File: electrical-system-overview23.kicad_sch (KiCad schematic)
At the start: 20 parts

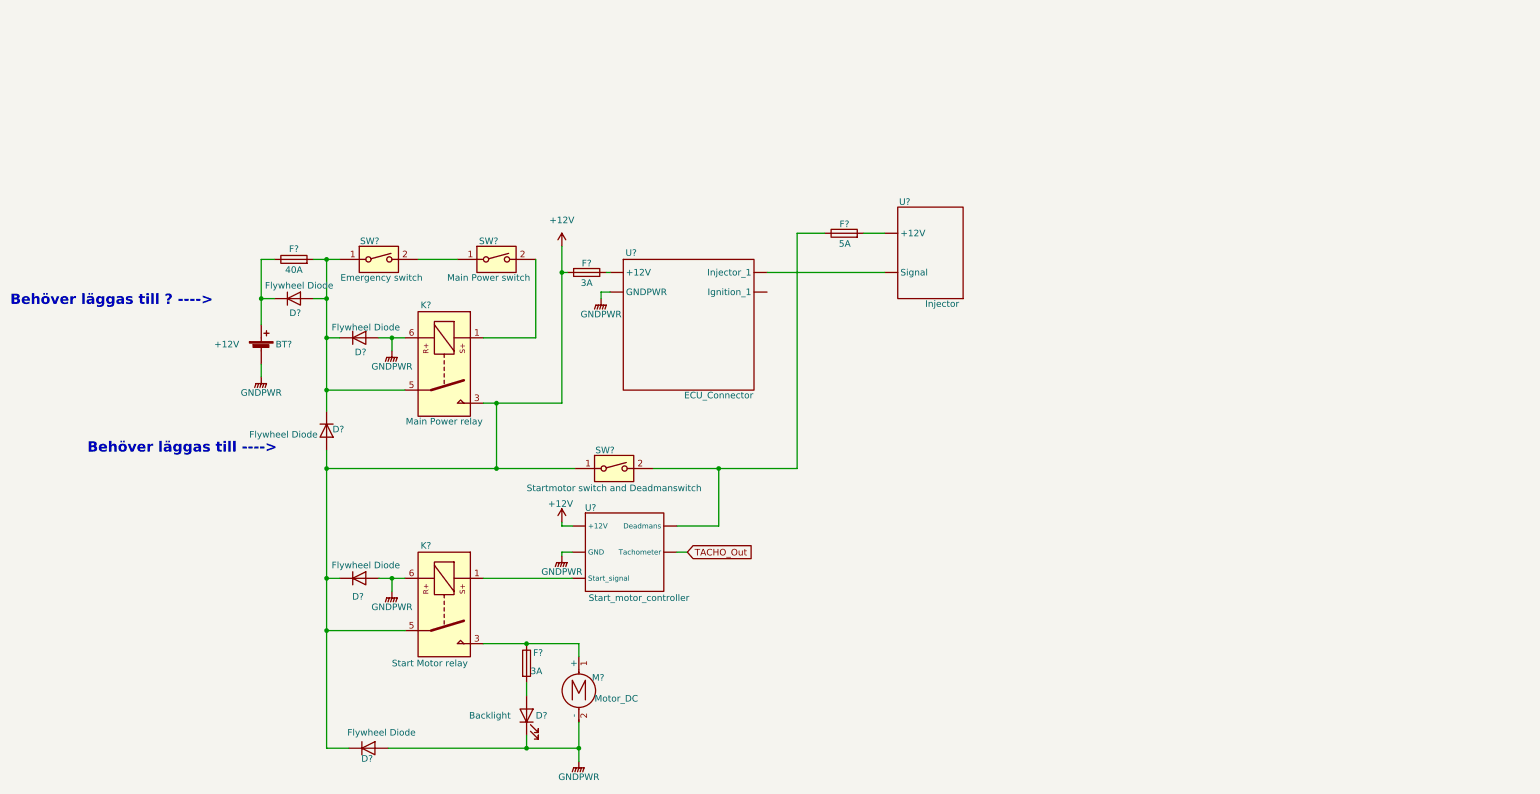
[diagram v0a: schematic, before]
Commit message: Fixed accuracy of system representation
- Changed position for flywheel diode
- Added more components to create a fuller picture
- Restructured the layout for easier reading
- Used two horizontal lines for power and ground
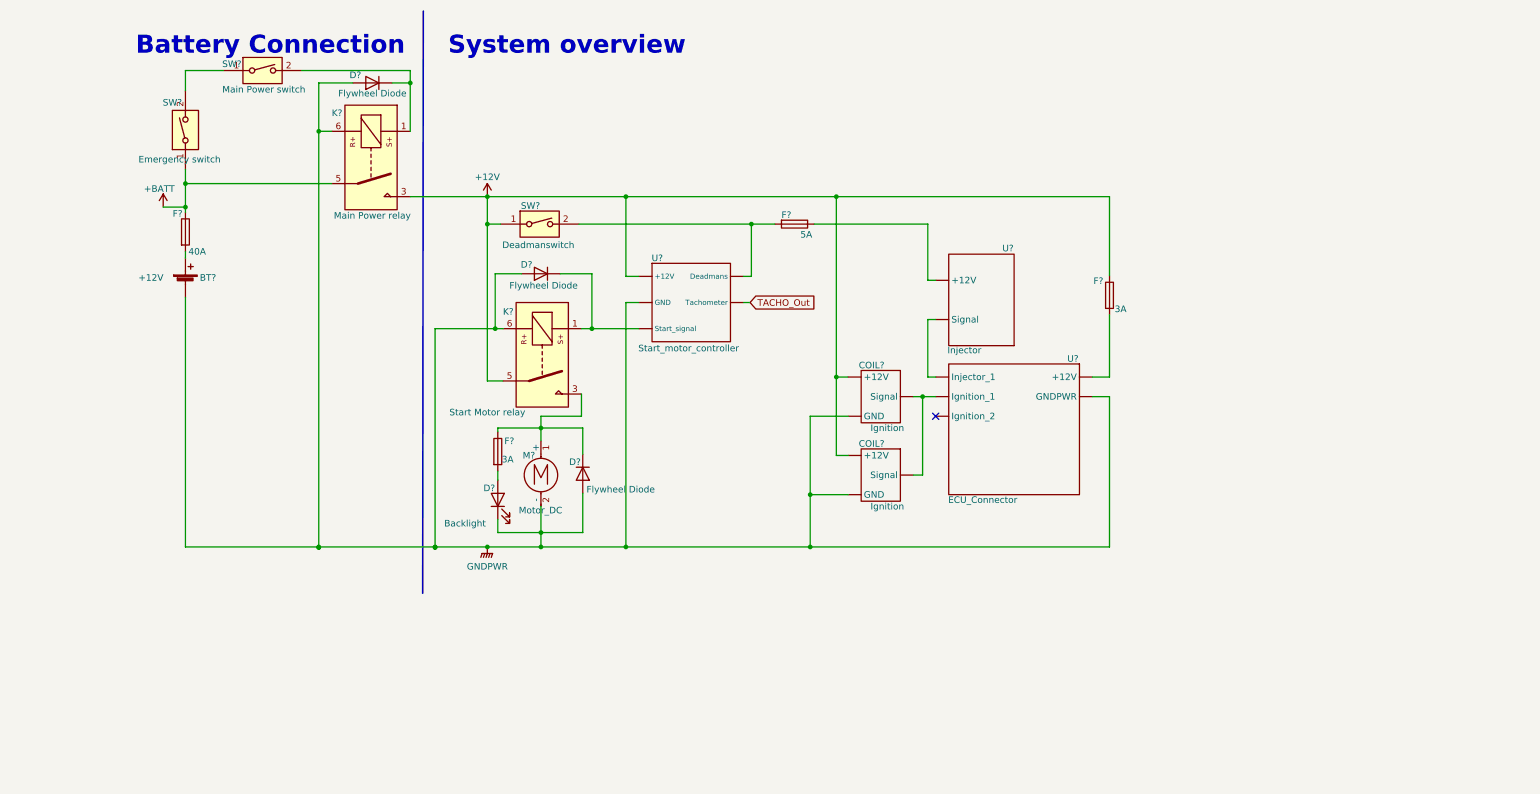
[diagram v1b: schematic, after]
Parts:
- removed D?: Backlight, symbol Device:LED
- removed D? (x4): Flywheel Diode, symbol Device:D
- removed F?: 3A, symbol Device:Fuse
- removed K?: Start Motor relay, Relay_THT:Relay_1P1T_NO_10x24x18.8mm_Panasonic_ADW11xxxxW_THT, symbol Relay:ADW11
- removed M?: Motor_DC, symbol Motor:Motor_DC
- removed SW?: Startmotor switch and Deadmanswitch, symbol Switch:SW_DIP_x01
- removed U?: Start_motor_controller, symbol electrical-system-overview23:Start_motor_controller
- added COIL? (x2): Ignition, symbol electrical-system-overview23:Ignition
- added D?: Backlight, symbol Device:LED
- added D? (x2): Flywheel Diode, symbol Device:D
- added F?: 3A, symbol Device:Fuse
- added K?: Start Motor relay, Relay_THT:Relay_1P1T_NO_10x24x18.8mm_Panasonic_ADW11xxxxW_THT, symbol Relay:ADW11
- added M?: Motor_DC, symbol Motor:Motor_DC
- added SW?: Deadmanswitch, symbol Switch:SW_DIP_x01
- added U?: Start_motor_controller, symbol electrical-system-overview23:Start_motor_controller
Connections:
- net +12V: now also F?.1, COIL?. (Signal), COIL?. (Signal), K?.5, SW?.1, U?. (Tachometer); no longer F?.2
- net GNDPWR: now also COIL?. (Signal), COIL?. (Signal), D?.1 (K), D?.2 (A), D?.2 (A), K?.6, M?.2 (-), U?. (Tachometer)
- net TACHO_Out: now also U?. (Tachometer)
- net at K?.1, SW?.2: now also D?.1 (K)
- net +BATT: now reaches K?.5, SW?.1
- net +BATT: now also F?.1; no longer D?.1 (K), F?.2
- net at F?.1: now also U?. (Signal)
- net at U?. (Signal): now also U?. (Injector_1); no longer F?.2
- net at BT?.1 (+): now also F?.2; no longer F?.1
- new net: D?.1 (K), F?.1, K?.3, M?.1 (+)
- new net: D?.2 (A), F?.2
- new net: F?.2, U?. (Injector_1)
- new net: F?.2, SW?.2, U?. (Tachometer)
- new net: COIL?. (Signal), COIL?. (Signal), U?. (Injector_1)
- new net: D?.1 (K), K?.1, U?. (Tachometer)
- no-connect marks 0 -> 1
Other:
- note added: "Battery Connection"
- note added: "System overview"
- note removed: "Behöver läggas till ---->"
- note removed: "Behöver läggas till ? ---->"
- moved on the sheet: BT?, D?, F?, K?, SW?, U?

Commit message: Added the Horn and Joulemeter to the schematic
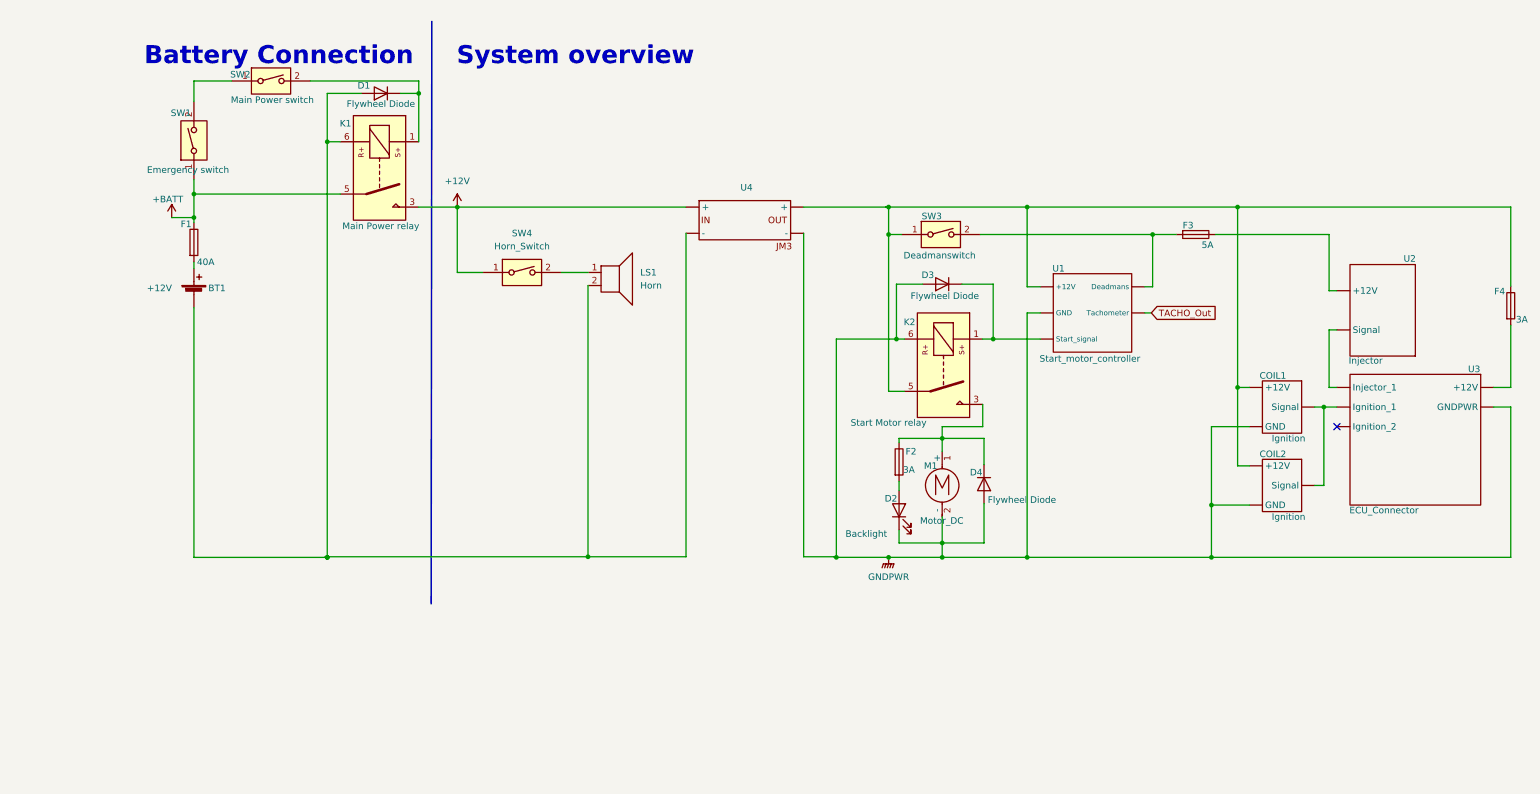
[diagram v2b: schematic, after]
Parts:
- added LS1: Horn, symbol Device:Speaker
- added SW4: Horn_Switch, symbol Switch:SW_DIP_x01
- added U4: ~, symbol Shell_Data_Telemetry:JM3
- gave numbers to parts that had none: 20
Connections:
- net +12V: now also SW4.1, U4. (-); no longer COIL1. (Signal), COIL2. (Signal), F4.1, K2.5, SW3.1, U1. (Tachometer)
- net GNDPWR: now also U4. (-); no longer BT1.2 (-), D1.2 (A), K1.6
- new net: BT1.2 (-), D1.2 (A), K1.6, LS1.2, U4. (-)
- new net: COIL1. (Signal), COIL2. (Signal), F4.1, K2.5, SW3.1, U1. (Tachometer), U4. (-)
- new net: LS1.1, SW4.2
- new net: COIL1. (Signal), COIL2. (Signal), U3. (Injector_1)
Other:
- moved on the sheet: BT1, COIL1, COIL2, D1, D2, D3, D4, F1, F2, F3, F4, K1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

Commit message: Shifted everything to better fit a 1.27mm grid
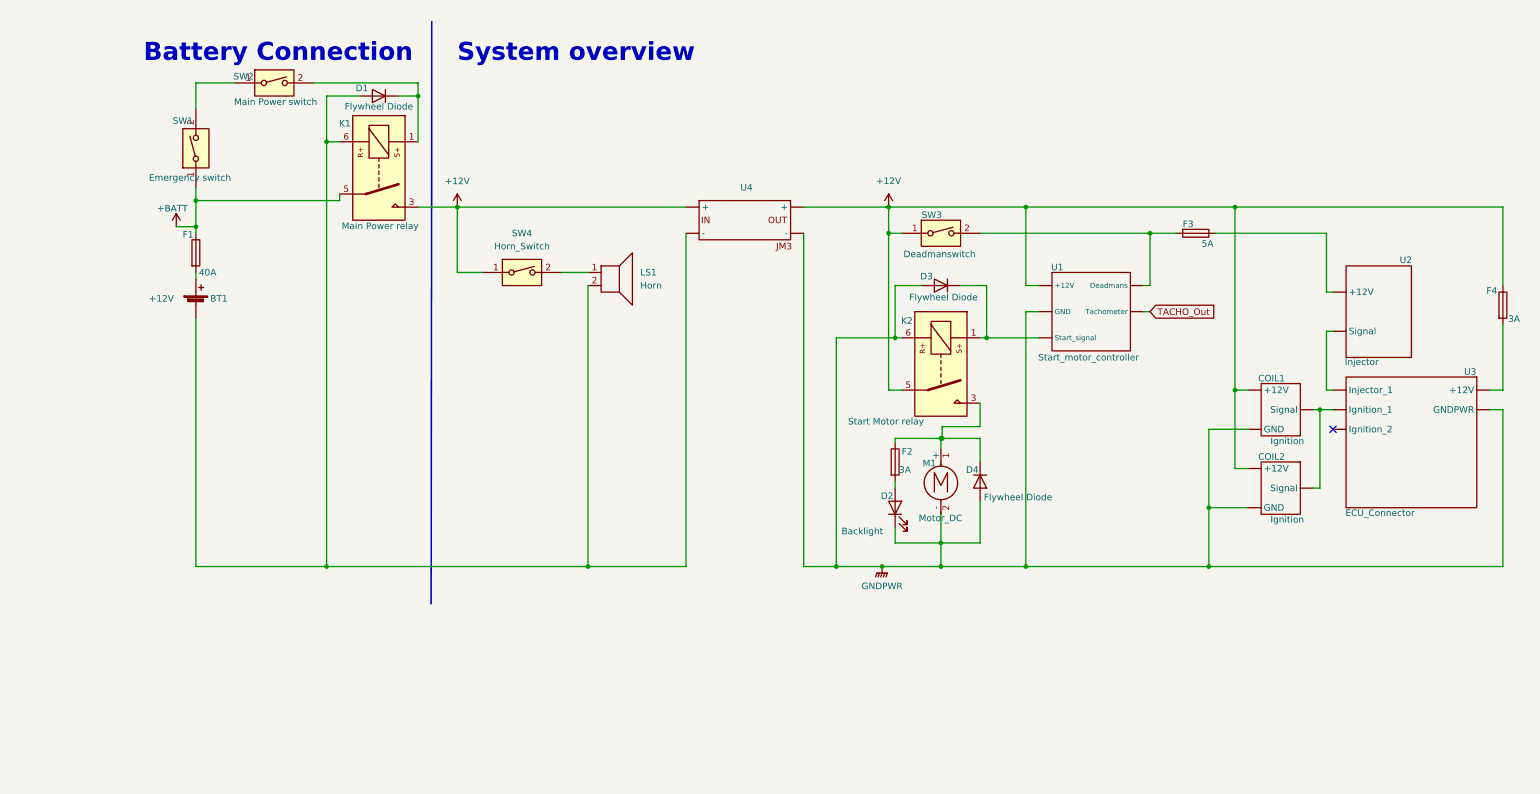
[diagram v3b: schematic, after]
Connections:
- new net: COIL1. (Signal), COIL2. (Signal), F4.1, K2.5, SW3.1, U1. (Tachometer), U4. (-)
- new net: COIL1. (Signal), COIL2. (Signal), U3. (Injector_1)
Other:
- moved on the sheet: BT1, COIL1, COIL2, D1, D2, D4, F1, F2, F4, K2, M1, SW1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
